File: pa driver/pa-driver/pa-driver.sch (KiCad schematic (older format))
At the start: 16 parts

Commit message: 9db PA Driver modification
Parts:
- added H5: M1, MountingHole:MountingHole_3.2mm_M3, symbol Mechanical:MountingHole
- added H6: M2, MountingHole:MountingHole_3.2mm_M3, symbol Mechanical:MountingHole
- added H7: M3, MountingHole:MountingHole_3.2mm_M3, symbol Mechanical:MountingHole
- added H8: M4, MountingHole:MountingHole_3.2mm_M3, symbol Mechanical:MountingHole
- C1, C2, C3: renamed from C?; footprint (none) -> Capacitor_THT:C_Disc_D5.1mm_W3.2mm_P5.00mm
- H1: renamed from H?; value MountingHole_Pad -> In-Sig; footprint (none) -> TestPoint:TestPoint_Pad_4.0x4.0mm
- H2: renamed from H?; value MountingHole_Pad -> GND Sig; footprint (none) -> TestPoint:TestPoint_Pad_4.0x4.0mm
- H3: renamed from H?; value MountingHole_Pad -> Out-sig; footprint (none) -> TestPoint:TestPoint_Pad_4.0x4.0mm
- H4: renamed from H?; value MountingHole_Pad -> GND; footprint (none) -> TestPoint:TestPoint_Pad_4.0x4.0mm
- J1: renamed from J?; footprint (none) -> Connector_PinHeader_2.54mm:PinHeader_1x02_P2.54mm_Vertical
- R1, R2, R3, R4, R5: renamed from R?; footprint (none) -> Resistor_THT:R_Axial_DIN0204_L3.6mm_D1.6mm_P5.08mm_Vertical
- T1: renamed from T?; footprint (none) -> pa-driver:Transformer2 1p 2s Binocular
- gave numbers to parts that had none: 2
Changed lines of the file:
@@
 $EndDescr
 $Comp
-L Transistor_BJT:PN2222A Q?
+L Transistor_BJT:PN2222A Q1
 U 1 1 5E5ED680
 P 4900 3450
-F 0 "Q?" H 5090 3496 50  0000 L CNN
+F 0 "Q1" H 5090 3496 50  0000 L CNN
 F 1 "PN2222A" H 5090 3405 50  0000 L CNN
 F 2 "Package_TO_SOT_THT:TO-92_Inline" H 5100 3375 50  0001 L CIN
@@
 $EndComp
 $Comp
-L Transistor_BJT:PN2222A Q?
+L Transistor_BJT:PN2222A Q2
 U 1 1 5E5EE68F
 P 8600 5150
-F 0 "Q?" H 8790 5196 50  0000 L CNN
+F 0 "Q2" H 8790 5196 50  0000 L CNN
 F 1 "PN2222A" H 8790 5105 50  0000 L CNN
 F 2 "Package_TO_SOT_THT:TO-92_Inline" H 8800 5075 50  0001 L CIN
@@
 $EndComp
 $Comp
-L Device:R R?
+L Device:R R1
 U 1 1 5E5EFD5B
 P 4000 3200
-F 0 "R?" H 4070 3246 50  0000 L CNN
+F 0 "R1" H 4070 3246 50  0000 L CNN
 F 1 "3.9k" H 4070 3155 50  0000 L CNN
-F 2 "" V 3930 3200 50  0001 C CNN
+F 2 "Resistor_THT:R_Axial_DIN0204_L3.6mm_D1.6mm_P5.08mm_Vertical" V 3930 3200 50  0001 C CNN
 F 3 "~" H 4000 3200 50  0001 C CNN
 	1    4000 3200
@@
 $EndComp
 $Comp
-L Device:R R?
+L Device:R R2
 U 1 1 5E5F0546
 P 4000 3700
-F 0 "R?" H 4070 3746 50  0000 L CNN
+F 0 "R2" H 4070 3746 50  0000 L CNN
 F 1 "1k" H 4070 3655 50  0000 L CNN
-F 2 "" V 3930 3700 50  0001 C CNN
+F 2 "Resistor_THT:R_Axial_DIN0204_L3.6mm_D1.6mm_P5.08mm_Vertical" V 3930 3700 50  0001 C CNN
 F 3 "~" H 4000 3700 50  0001 C CNN
 	1    4000 3700
@@
 $EndComp
 $Comp
-L Device:R R?
+L Device:R R4
 U 1 1 5E5F0B81
 P 5000 4250
-F 0 "R?" H 5070 4296 50  0000 L CNN
+F 0 "R4" H 5070 4296 50  0000 L CNN
 F 1 "47ohm" H 5070 4205 50  0000 L CNN
-F 2 "" V 4930 4250 50  0001 C CNN
+F 2 "Resistor_THT:R_Axial_DIN0204_L3.6mm_D1.6mm_P5.08mm_Vertical" V 4930 4250 50  0001 C CNN
 F 3 "~" H 5000 4250 50  0001 C CNN
 	1    5000 4250
@@
 $EndComp
 $Comp
-L Device:R R?
+L Device:R R3
 U 1 1 5E5F110C
 P 4350 3450
-F 0 "R?" V 4143 3450 50  0000 C CNN
+F 0 "R3" V 4143 3450 50  0000 C CNN
 F 1 "4.7 ohm" V 4234 3450 50  0000 C CNN
-F 2 "" V 4280 3450 50  0001 C CNN
+F 2 "Resistor_THT:R_Axial_DIN0204_L3.6mm_D1.6mm_P5.08mm_Vertical" V 4280 3450 50  0001 C CNN
 F 3 "~" H 4350 3450 50  0001 C CNN
 	1    4350 3450
@@
 $EndComp
 $Comp
-L Device:R R?
+L Device:R R5
 U 1 1 5E5F27A9
 P 8150 5150
-F 0 "R?" V 7943 5150 50  0000 C CNN
+F 0 "R5" V 7943 5150 50  0000 C CNN
 F 1 "R" V 8034 5150 50  0000 C CNN
-F 2 "" V 8080 5150 50  0001 C CNN
+F 2 "Resistor_THT:R_Axial_DIN0204_L3.6mm_D1.6mm_P5.08mm_Vertical" V 8080 5150 50  0001 C CNN
 F 3 "~" H 8150 5150 50  0001 C CNN
 	1    8150 5150
@@
 $EndComp
 $Comp
-L Device:C C?
+L Device:C C1
 U 1 1 5E5F345F
 P 2600 2700
-F 0 "C?" V 2348 2700 50  0000 C CNN
+F 0 "C1" V 2348 2700 50  0000 C CNN
 F 1 "100nf" V 2439 2700 50  0000 C CNN
-F 2 "" H 2638 2550 50  0001 C CNN
+F 2 "Capacitor_THT:C_Disc_D5.1mm_W3.2mm_P5.00mm" H 2638 2550 50  0001 C CNN
 F 3 "~" H 2600 2700 50  0001 C CNN
 	1    2600 2700
@@
 $EndComp
 $Comp
-L Device:C C?
+L Device:C C2
 U 1 1 5E5F3DA9
 P 2600 3450
-F 0 "C?" V 2348 3450 50  0000 C CNN
+F 0 "C2" V 2348 3450 50  0000 C CNN
 F 1 "100nf" V 2439 3450 50  0000 C CNN
-F 2 "" H 2638 3300 50  0001 C CNN
+F 2 "Capacitor_THT:C_Disc_D5.1mm_W3.2mm_P5.00mm" H 2638 3300 50  0001 C CNN
 F 3 "~" H 2600 3450 50  0001 C CNN
 	1    2600 3450
@@
 $EndComp
 $Comp
-L Device:C C?
+L Device:C C3
 U 1 1 5E5F4293
 P 7700 3250
-F 0 "C?" V 7448 3250 50  0000 C CNN
+F 0 "C3" V 7448 3250 50  0000 C CNN
 F 1 "100nf" V 7539 3250 50  0000 C CNN
-F 2 "" H 7738 3100 50  0001 C CNN
+F 2 "Capacitor_THT:C_Disc_D5.1mm_W3.2mm_P5.00mm" H 7738 3100 50  0001 C CNN
 F 3 "~" H 7700 3250 50  0001 C CNN
 	1    7700 3250
@@
 $EndComp
 $Comp
-L power:+12V #PWR?
+L power:+12V #PWR0101
 U 1 1 5E5F4C66
 P 5950 2100
-F 0 "#PWR?" H 5950 1950 50  0001 C CNN
+F 0 "#PWR0101" H 5950 1950 50  0001 C CNN
 F 1 "+12V" V 5965 2228 50  0000 L CNN
 F 2 "" H 5950 2100 50  0001 C CNN
@@
 $EndComp
 $Comp
-L power:GND #PWR?
+L power:GND #PWR0102
 U 1 1 5E5F5400
 P 8550 4050
-F 0 "#PWR?" H 8550 3800 50  0001 C CNN
+F 0 "#PWR0102" H 8550 3800 50  0001 C CNN
 F 1 "GND" H 8555 3877 50  0000 C CNN
 F 2 "" H 8550 4050 50  0001 C CNN
@@
 $EndComp
 $Comp
-L Device:Transformer_1P_2S T?
+L Device:Transformer_1P_2S T1
 U 1 1 5E5F77E7
 P 4600 2500
-F 0 "T?" H 4600 3081 50  0000 C CNN
+F 0 "T1" H 4600 3081 50  0000 C CNN
 F 1 "Transformer_1P_2S" H 4600 2990 50  0000 C CNN
-F 2 "" H 4600 2500 50  0001 C CNN
+F 2 "pa-driver:Transformer2 1p 2s Binocular" H 4600 2500 50  0001 C CNN
 F 3 "~" H 4600 2500 50  0001 C CNN
 	1    4600 2500
@@
 	2750 2700 4200 2700
 $Comp
-L power:GND #PWR?
+L power:GND #PWR0103
 U 1 1 5E5FF74F
 P 5000 4750
-F 0 "#PWR?" H 5000 4500 50  0001 C CNN
+F 0 "#PWR0103" H 5000 4500 50  0001 C CNN
 F 1 "GND" H 5005 4577 50  0000 C CNN
 F 2 "" H 5000 4750 50  0001 C CNN
@@
 	5000 4500 5000 4750
 $Comp
-L power:GND #PWR?
+L power:GND #PWR0104
 U 1 1 5E6011B0
 P 2200 3450
-F 0 "#PWR?" H 2200 3200 50  0001 C CNN
+F 0 "#PWR0104" H 2200 3200 50  0001 C CNN
 F 1 "GND" V 2205 3322 50  0000 R CNN
 F 2 "" H 2200 3450 50  0001 C CNN
@@
 Connection ~ 5350 2100
 $Comp
-L Mechanical:MountingHole_Pad H?
+L Mechanical:MountingHole_Pad H1
 U 1 1 5E607763
 P 2200 2600
-F 0 "H?" H 2300 2649 50  0000 L CNN
-F 1 "MountingHole_Pad" H 2300 2558 50  0000 L CNN
-F 2 "" H 2200 2600 50  0001 C CNN
+F 0 "H1" H 2300 2649 50  0000 L CNN
+F 1 "In-Sig" H 2300 2558 50  0000 L CNN
+F 2 "TestPoint:TestPoint_Pad_4.0x4.0mm" H 2200 2600 50  0001 C CNN
 F 3 "~" H 2200 2600 50  0001 C CNN
 	1    2200 2600
@@
 $EndComp
 $Comp
-L Mechanical:MountingHole_Pad H?
+L Mechanical:MountingHole_Pad H2
 U 1 1 5E607FA9
 P 2200 3350
-F 0 "H?" H 2300 3399 50  0000 L CNN
-F 1 "MountingHole_Pad" H 2300 3308 50  0000 L CNN
-F 2 "" H 2200 3350 50  0001 C CNN
+F 0 "H2" H 2300 3399 50  0000 L CNN
+F 1 "GND Sig" H 2300 3308 50  0000 L CNN
+F 2 "TestPoint:TestPoint_Pad_4.0x4.0mm" H 2200 3350 50  0001 C CNN
 F 3 "~" H 2200 3350 50  0001 C CNN
 	1    2200 3350
@@
 $EndComp
 $Comp
-L Mechanical:MountingHole_Pad H?
+L Mechanical:MountingHole_Pad H3
 U 1 1 5E6085AB
 P 8500 3250
-F 0 "H?" V 8454 3400 50  0000 L CNN
-F 1 "MountingHole_Pad" V 8545 3400 50  0000 L CNN
-F 2 "" H 8500 3250 50  0001 C CNN
+F 0 "H3" V 8454 3400 50  0000 L CNN
+F 1 "Out-sig" V 8545 3400 50  0000 L CNN
+F 2 "TestPoint:TestPoint_Pad_4.0x4.0mm" H 8500 3250 50  0001 C CNN
 F 3 "~" H 8500 3250 50  0001 C CNN
 	1    8500 3250
@@
 $EndComp
 $Comp
-L Mechanical:MountingHole_Pad H?
+L Mechanical:MountingHole_Pad H4
 U 1 1 5E608EA9
 P 8550 3950
-F 0 "H?" H 8650 3999 50  0000 L CNN
-F 1 "MountingHole_Pad" H 8650 3908 50  0000 L CNN
-F 2 "" H 8550 3950 50  0001 C CNN
+F 0 "H4" H 8650 3999 50  0000 L CNN
+F 1 "GND" H 8650 3908 50  0000 L CNN
+F 2 "TestPoint:TestPoint_Pad_4.0x4.0mm" H 8550 3950 50  0001 C CNN
 F 3 "~" H 8550 3950 50  0001 C CNN
 	1    8550 3950
@@
 T1: 1 - 3 turns\n      2 - 5 turns\n      3 - 1 turn
 $Comp
-L Connector:Conn_01x02_Female J?
+L Connector:Conn_01x02_Female J1
 U 1 1 5E61225F
 P 8050 4400
-F 0 "J?" V 7896 4448 50  0000 L CNN
+F 0 "J1" V 7896 4448 50  0000 L CNN
 F 1 "Conn_01x02_Female" V 7987 4448 50  0000 L CNN
-F 2 "" H 8050 4400 50  0001 C CNN
+F 2 "Connector_PinHeader_2.54mm:PinHeader_1x02_P2.54mm_Vertical" H 8050 4400 50  0001 C CNN
 F 3 "~" H 8050 4400 50  0001 C CNN
 	1    8050 4400
@@
 $EndComp
 $Comp
-L power:+12V #PWR?
+L power:+12V #PWR0105
 U 1 1 5E61376B
 P 7950 4200
-F 0 "#PWR?" H 7950 4050 50  0001 C CNN
+F 0 "#PWR0105" H 7950 4050 50  0001 C CNN
 F 1 "+12V" H 7965 4373 50  0000 C CNN
 F 2 "" H 7950 4200 50  0001 C CNN
@@
 Text Notes 7850 4600 0    50   ~ 0
 12v input
+$Comp
+L Mechanical:MountingHole H5
+U 1 1 5E67053F
+P 9400 900
+F 0 "H5" H 9500 946 50  0000 L CNN
+F 1 "M1" H 9500 855 50  0000 L CNN
+F 2 "MountingHole:MountingHole_3.2mm_M3" H 9400 900 50  0001 C CNN
+F 3 "~" H 9400 900 50  0001 C CNN
+	1    9400 900
+	1    0    0    -1
+$EndComp
+$Comp
+L Mechanical:MountingHole H6
+U 1 1 5E670E6D
+P 9400 1200
+F 0 "H6" H 9500 1246 50  0000 L CNN
+F 1 "M2" H 9500 1155 50  0000 L CNN
+F 2 "MountingHole:MountingHole_3.2mm_M3" H 9400 1200 50  0001 C CNN
+F 3 "~" H 9400 1200 50  0001 C CNN
+	1    9400 1200
+	1    0    0    -1
+$EndComp
+$Comp
+L Mechanical:MountingHole H7
+U 1 1 5E671848
+P 9400 1500
+F 0 "H7" H 9500 1546 50  0000 L CNN
+F 1 "M3" H 9500 1455 50  0000 L CNN
+F 2 "MountingHole:MountingHole_3.2mm_M3" H 9400 1500 50  0001 C CNN
+F 3 "~" H 9400 1500 50  0001 C CNN
+	1    9400 1500
+	1    0    0    -1
+$EndComp
+$Comp
+L Mechanical:MountingHole H8
+U 1 1 5E671EEE
+P 9400 1800
+F 0 "H8" H 9500 1846 50  0000 L CNN
+F 1 "M4" H 9500 1755 50  0000 L CNN
+F 2 "MountingHole:MountingHole_3.2mm_M3" H 9400 1800 50  0001 C CNN
+F 3 "~" H 9400 1800 50  0001 C CNN
+	1    9400 1800
+	1    0    0    -1
+$EndComp
 $EndSCHEMATC

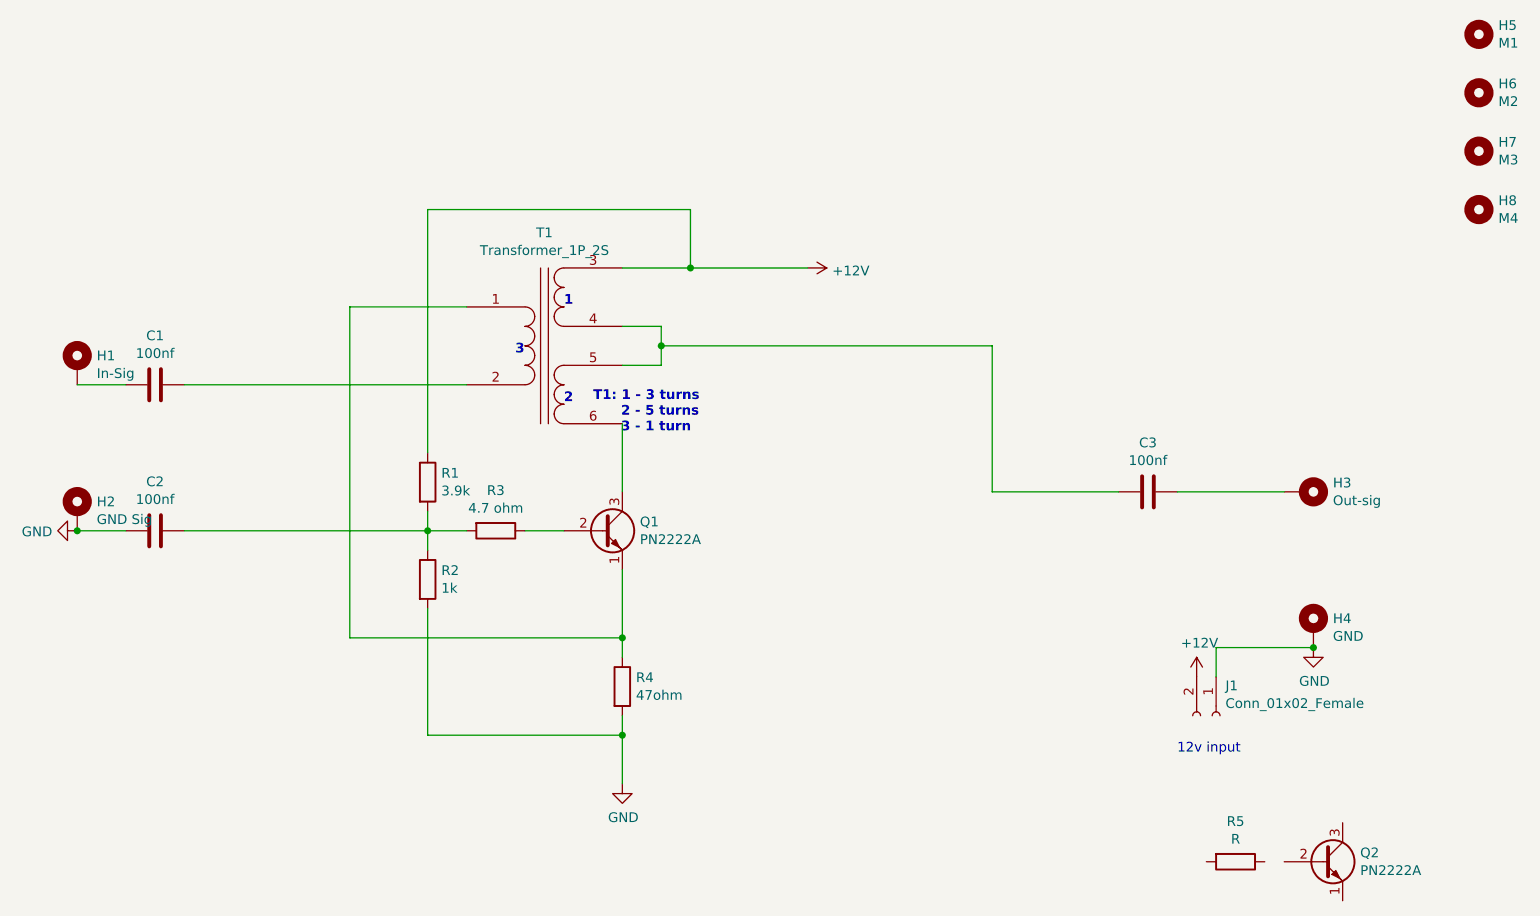
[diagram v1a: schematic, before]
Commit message: Modif to PA driver
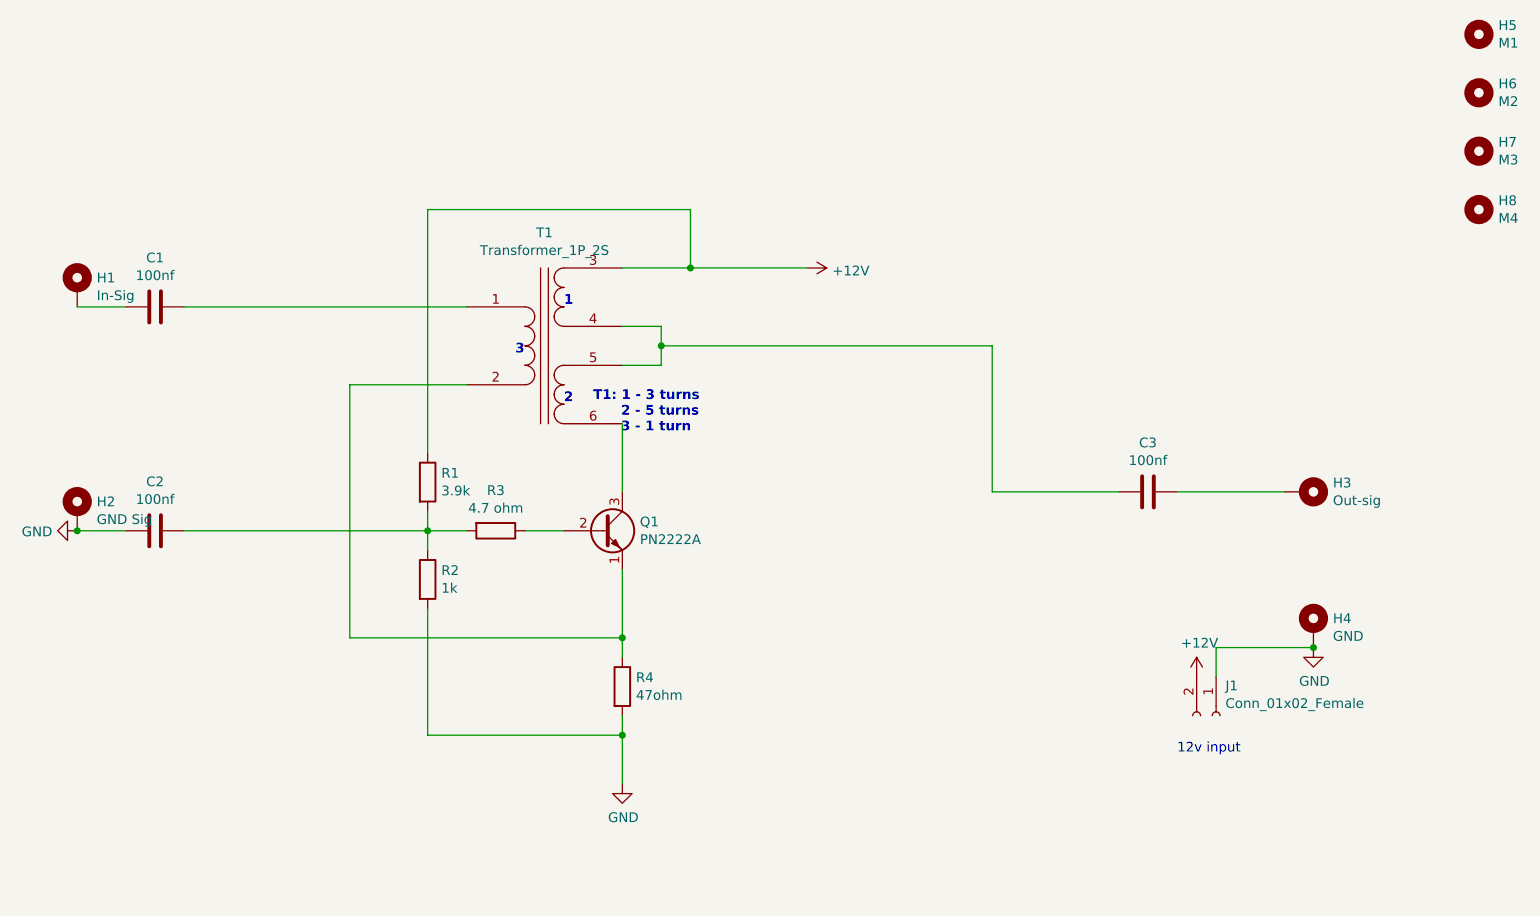
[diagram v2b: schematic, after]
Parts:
- removed Q2: PN2222A, Package_TO_SOT_THT:TO-92_Inline, symbol Transistor_BJT:PN2222A
- removed R5: R, Resistor_THT:R_Axial_DIN0204_L3.6mm_D1.6mm_P5.08mm_Vertical, symbol Device:R
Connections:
- net at Q1.1 (E), R4.1: now also T1.2 (AB); no longer T1.1 (AA)
- net at C1.1: now also T1.1 (AA); no longer T1.2 (AB)
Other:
- moved on the sheet: C1, H1
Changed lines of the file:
@@
-$EndComp
-$Comp
-L Transistor_BJT:PN2222A Q2
-U 1 1 5E5EE68F
-P 8600 5150
-F 0 "Q2" H 8790 5196 50  0000 L CNN
-F 1 "PN2222A" H 8790 5105 50  0000 L CNN
-F 2 "Package_TO_SOT_THT:TO-92_Inline" H 8800 5075 50  0001 L CIN
-F 3 "http://www.fairchildsemi.com/ds/PN/PN2222A.pdf" H 8600 5150 50  0001 L CNN
-	1    8600 5150
-	1    0    0    -1
 $EndComp
 $Comp
@@
 $EndComp
 $Comp
-L Device:R R5
-U 1 1 5E5F27A9
-P 8150 5150
-F 0 "R5" V 7943 5150 50  0000 C CNN
-F 1 "R" V 8034 5150 50  0000 C CNN
-F 2 "Resistor_THT:R_Axial_DIN0204_L3.6mm_D1.6mm_P5.08mm_Vertical" V 8080 5150 50  0001 C CNN
-F 3 "~" H 8150 5150 50  0001 C CNN
-	1    8150 5150
-	0    1    1    0
-$EndComp
-$Comp
 L Device:C C1
 U 1 1 5E5F345F
-P 2600 2700
-F 0 "C1" V 2348 2700 50  0000 C CNN
-F 1 "100nf" V 2439 2700 50  0000 C CNN
-F 2 "Capacitor_THT:C_Disc_D5.1mm_W3.2mm_P5.00mm" H 2638 2550 50  0001 C CNN
-F 3 "~" H 2600 2700 50  0001 C CNN
-	1    2600 2700
+P 2600 2300
+F 0 "C1" V 2348 2300 50  0000 C CNN
+F 1 "100nf" V 2439 2300 50  0000 C CNN
+F 2 "Capacitor_THT:C_Disc_D5.1mm_W3.2mm_P5.00mm" H 2638 2150 50  0001 C CNN
+F 3 "~" H 2600 2300 50  0001 C CNN
+	1    2600 2300
 	0    1    1    0
 $EndComp
@@
 	4000 3450 4000 3550
 Wire Wire Line
-	4200 2300 3600 2300
-Wire Wire Line
-	3600 2300 3600 4000
-Wire Wire Line
 	3600 4000 5000 4000
 Wire Wire Line
@@
 Wire Wire Line
 	2750 3450 4000 3450
-Wire Wire Line
-	2750 2700 4200 2700
 $Comp
 L power:GND #PWR0103
@@
 L Mechanical:MountingHole_Pad H1
 U 1 1 5E607763
-P 2200 2600
-F 0 "H1" H 2300 2649 50  0000 L CNN
-F 1 "In-Sig" H 2300 2558 50  0000 L CNN
-F 2 "TestPoint:TestPoint_Pad_4.0x4.0mm" H 2200 2600 50  0001 C CNN
-F 3 "~" H 2200 2600 50  0001 C CNN
-	1    2200 2600
+P 2200 2200
+F 0 "H1" H 2300 2249 50  0000 L CNN
+F 1 "In-Sig" H 2300 2158 50  0000 L CNN
+F 2 "TestPoint:TestPoint_Pad_4.0x4.0mm" H 2200 2200 50  0001 C CNN
+F 3 "~" H 2200 2200 50  0001 C CNN
+	1    2200 2200
 	1    0    0    -1
 $EndComp
@@
 Connection ~ 2200 3450
 Wire Wire Line
-	2200 2700 2450 2700
+	2200 2300 2450 2300
 Text Notes 4700 2300 0    50   ~ 10
 1
@@
 	1    0    0    -1
 $EndComp
+Wire Wire Line
+	4200 2700 3600 2700
+Wire Wire Line
+	3600 2700 3600 4000
+Wire Wire Line
+	2750 2300 4200 2300
 $EndSCHEMATC
